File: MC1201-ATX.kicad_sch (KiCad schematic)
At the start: 246 parts, among them J1 PLD-16, J2 PLD-16, J3 PLD-16, J4 ATX-20, J5 Conn_01x01_Pin, J6 Conn_01x01_Pin, P1 Conn_01x01_Pin, P10 Conn_01x01_Pin, P11 Conn_01x01_Pin, P12 Conn_01x01_Pin, P13 Conn_01x01_Pin, P14 Conn_01x01_Pin, P15 Conn_01x01_Pin, P16 Conn_01x01_Pin, P17 Conn_01x01_Pin, P18 Conn_01x01_Pin, P2 Conn_01x01_Pin, P3 Conn_01x01_Pin, P4 Conn_01x01_Pin, P5 Conn_01x01_Pin, P6 Conn_01x01_Pin, P7 Conn_01x01_Pin, P8 Conn_01x01_Pin, P9 Conn_01x01_Pin, Q1 BC547, X2 AFPC, X3 QBUS_DWK_64Pin_MBT

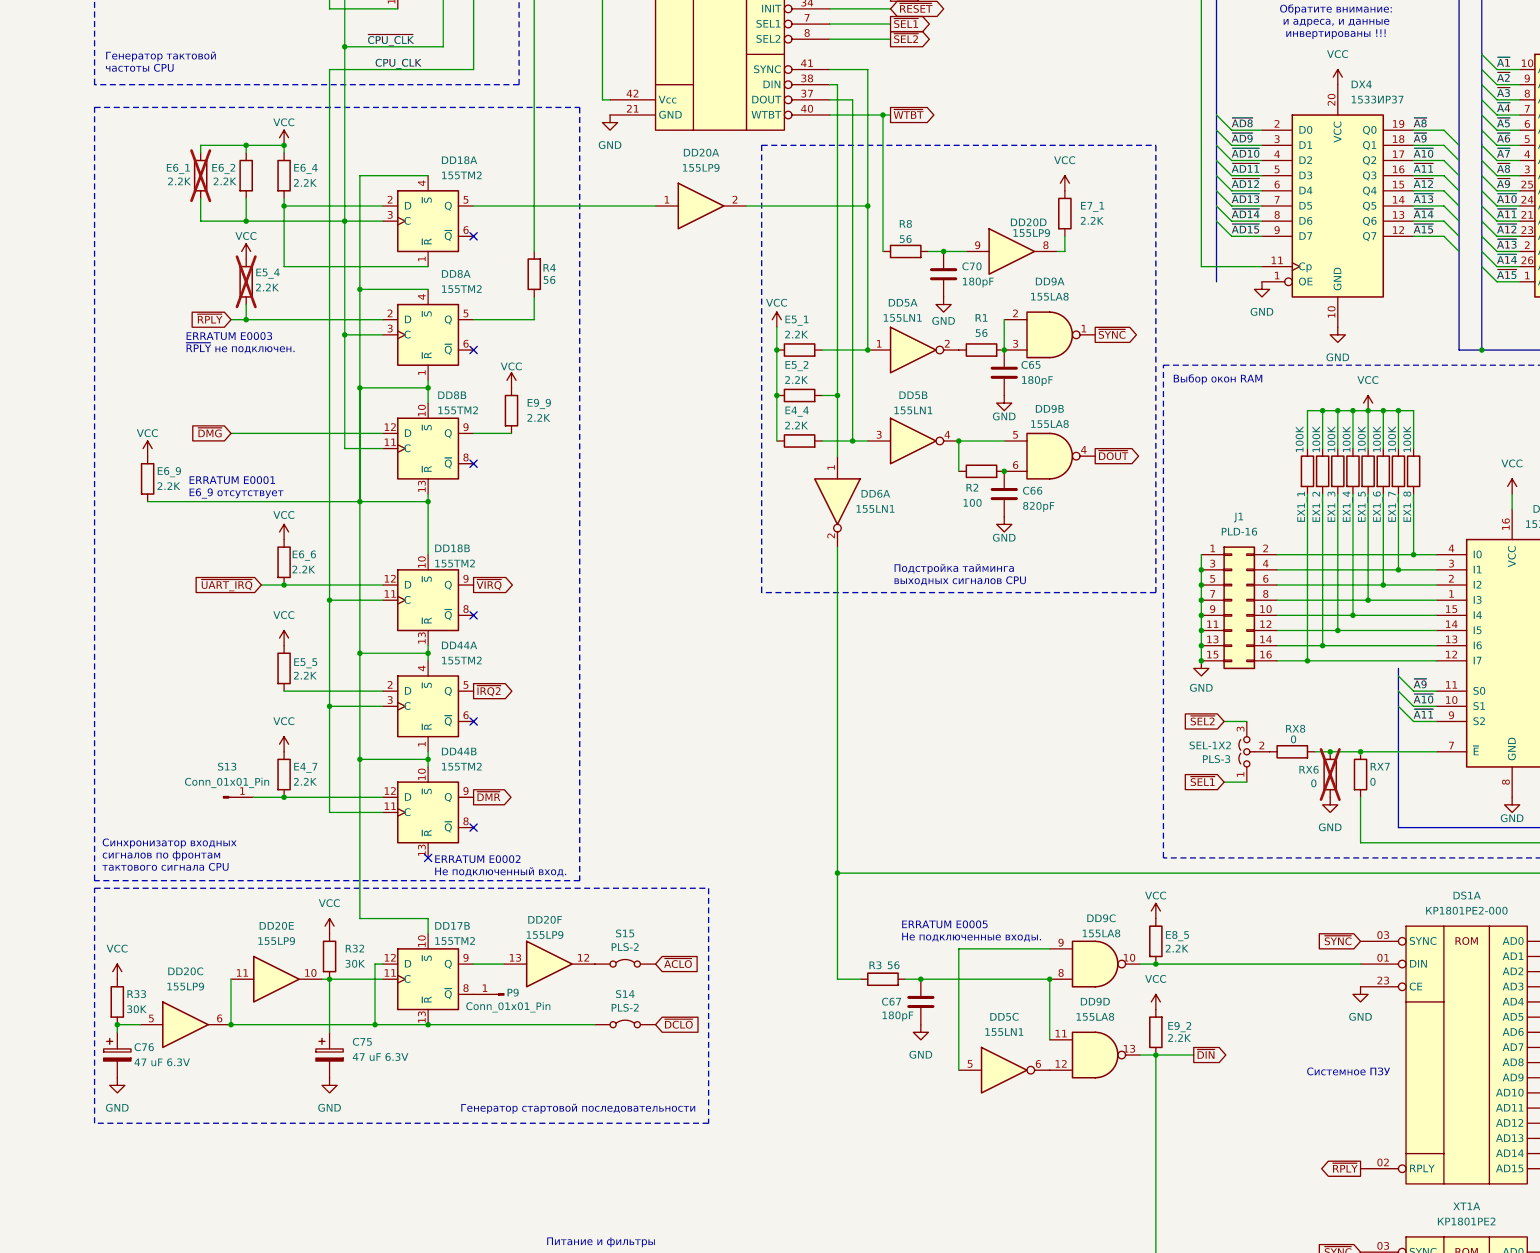
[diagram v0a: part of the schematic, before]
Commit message: Some more info
More DNP components with explanations why.
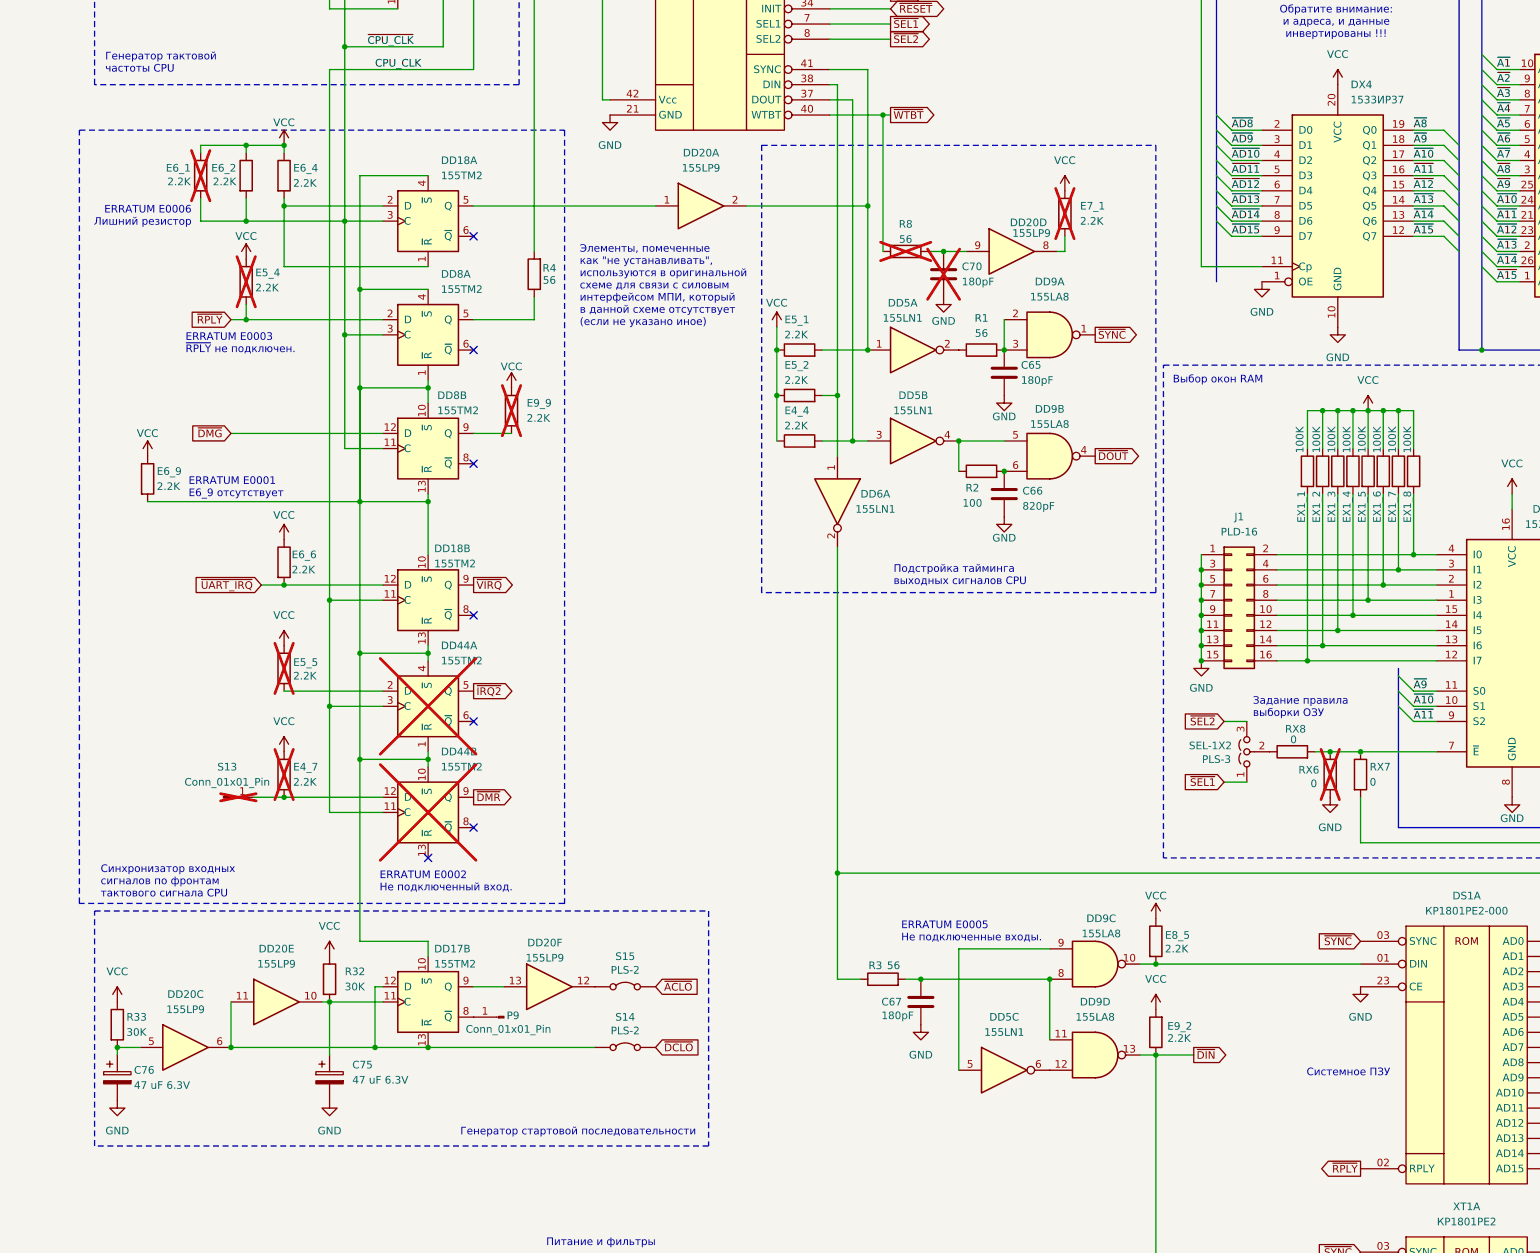
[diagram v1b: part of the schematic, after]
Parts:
- C70, DD44, E4_7, E5_5, E7_1, E9_9, R8, S13: now not fitted
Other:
- note added: "ERRATUM E0006 Лишний резистор"
- note added: "Задание правила выборки ОЗУ"
- note added: "Элементы, помеченные как "не устанавливать", используются в оригинальной схеме для связи с силовым интерфейсом МПИ, который в данной схеме отсутствует (если не указано иное)"
- moved on the sheet: C75, C76, DD17B, DD20C, DD20E, DD20F, P9, R32, R33, S14, S15

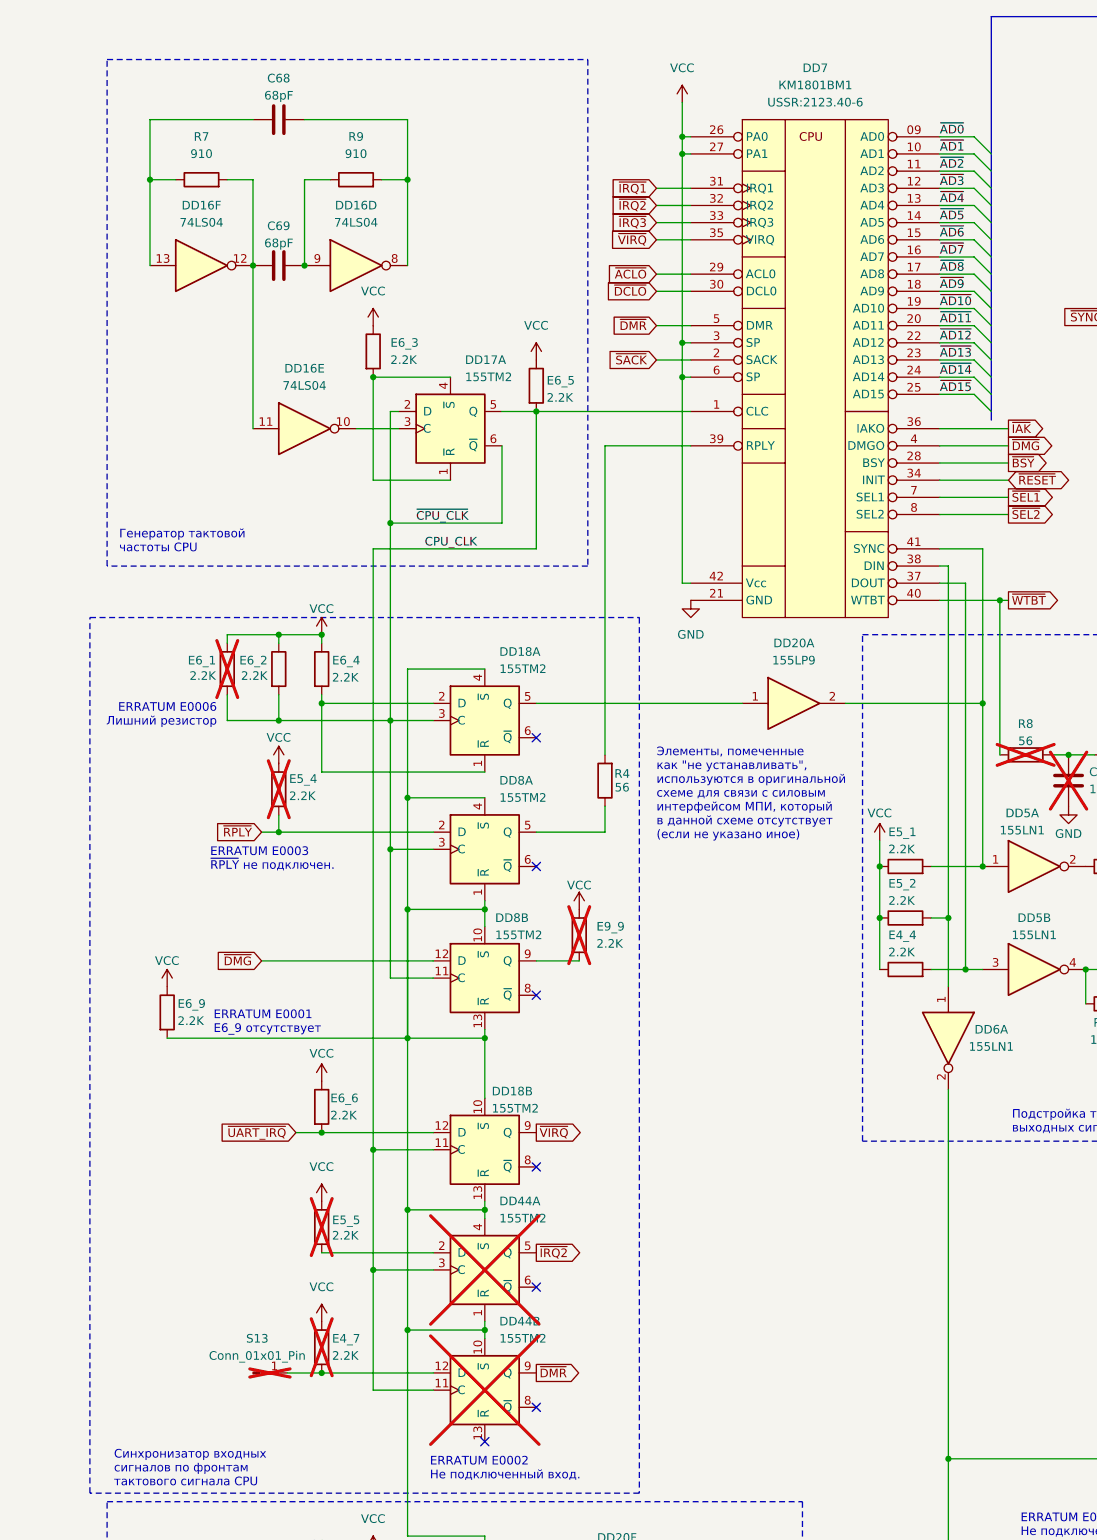
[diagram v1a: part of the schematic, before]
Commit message: Some clarifications
Figured out "STANDARD_CLOCK" solder bridge
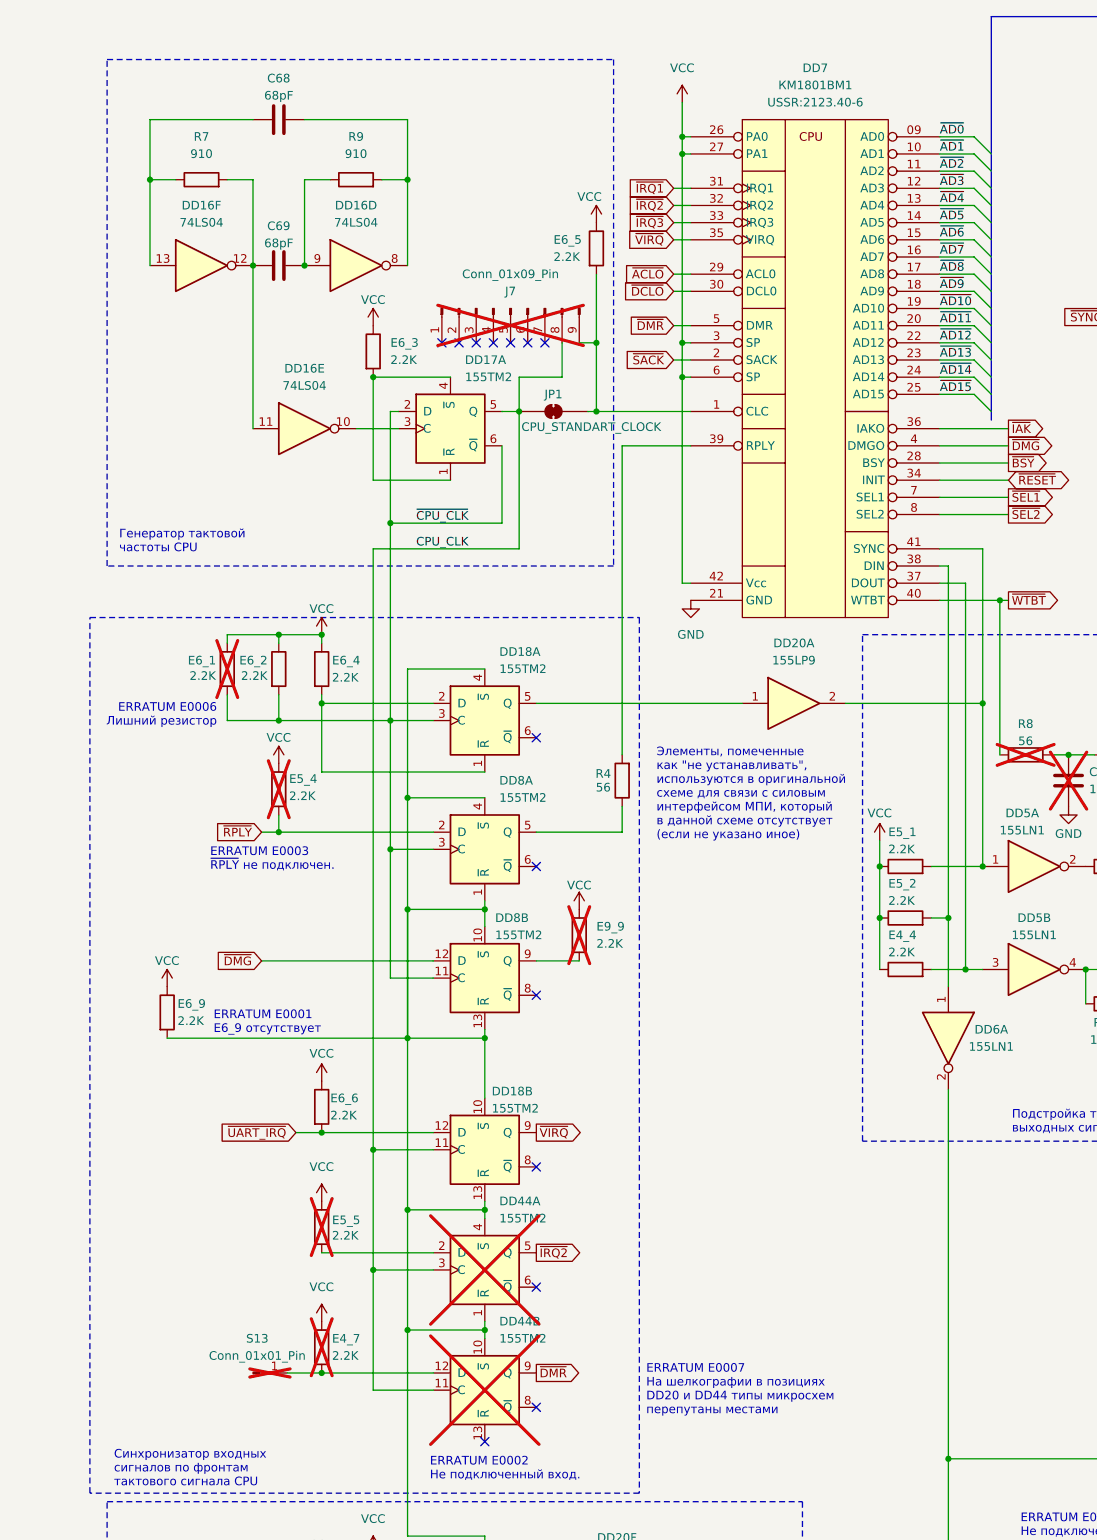
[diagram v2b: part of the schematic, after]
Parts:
- added J7: Conn_01x09_Pin, Connector_PinHeader_2.54mm:PinHeader_1x09_P2.54mm_Vertical, symbol Connector:Conn_01x09_Pin
- added JP1: CPU_STANDART_CLOCK, Jumper:SolderJumper-2_P1.3mm_Bridged_Pad1.0x1.5mm, symbol Jumper:SolderJumper_2_Bridged
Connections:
- net CPU_CLK: now also J7.8 (Pin_8), JP1.1 (A); no longer DD7.1 (CLC), E6_5.2
- new net: DD7.1 (CLC), E6_5.2, J7.9 (Pin_9), JP1.2 (B)
- no-connect marks 28 -> 35
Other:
- note added: "ERRATUM E0007 На шелкографии в позициях DD20 и DD44 типы микросхем перепутаны местами"
- moved on the sheet: E6_5, R4

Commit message: Understood address space
Added memory map info
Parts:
- XT1: value КР1801РЕ2 -> КР1801РЕ2-013
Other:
- note added: "Пользовательское ПЗУ Адреса 140000_{8}-157777_{8} (для бейсика)"
- note added: "Регистр начального пуска. Стартовый адрес 160000 (используется только старший байт) Состояние SA1 можно прочесть программно"
- note added: "Селектор верхних адресов ~{MMIO} = (ADDR >= 16xxxx_{8})"
- note added: "Системное ПЗУ Адреса 160000_{8}-177777_{8}"
- note removed: "Пользовательское ПЗУ"
- note removed: "Системное ПЗУ"
- moved on the sheet: DD10C, DD15A, DD15B, DD15C, DD15D, DD15E, DD15F, DD6B, SA1
